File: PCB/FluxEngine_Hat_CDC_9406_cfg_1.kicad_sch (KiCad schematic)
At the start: 6 parts, among them J1 CY8CKIT-059, P1 FDD_IBMPC_host, P2 FDD_SA800_host

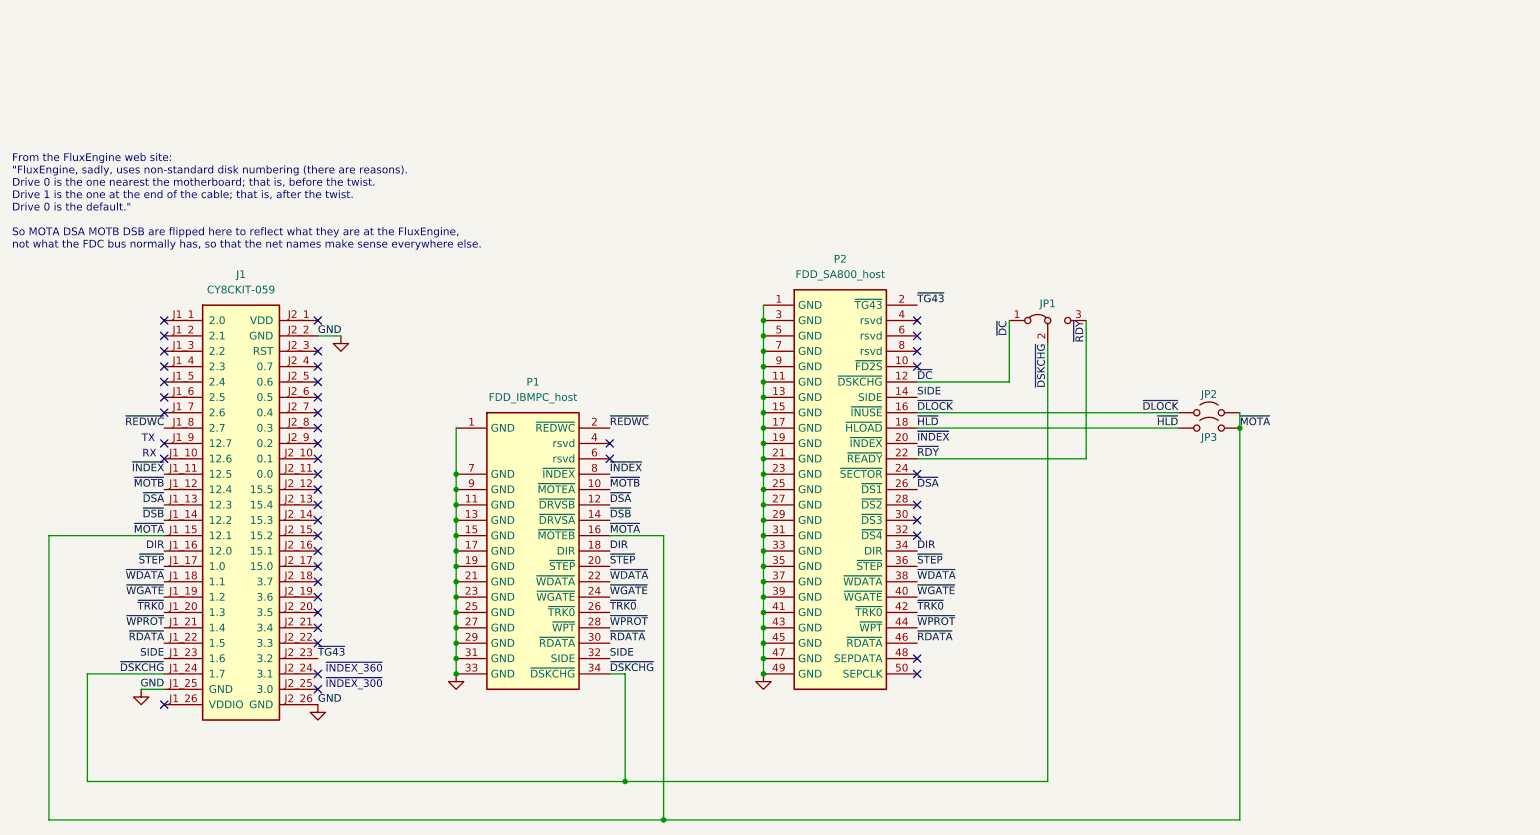
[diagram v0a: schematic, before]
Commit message: add CDC9406 type 1 & 2
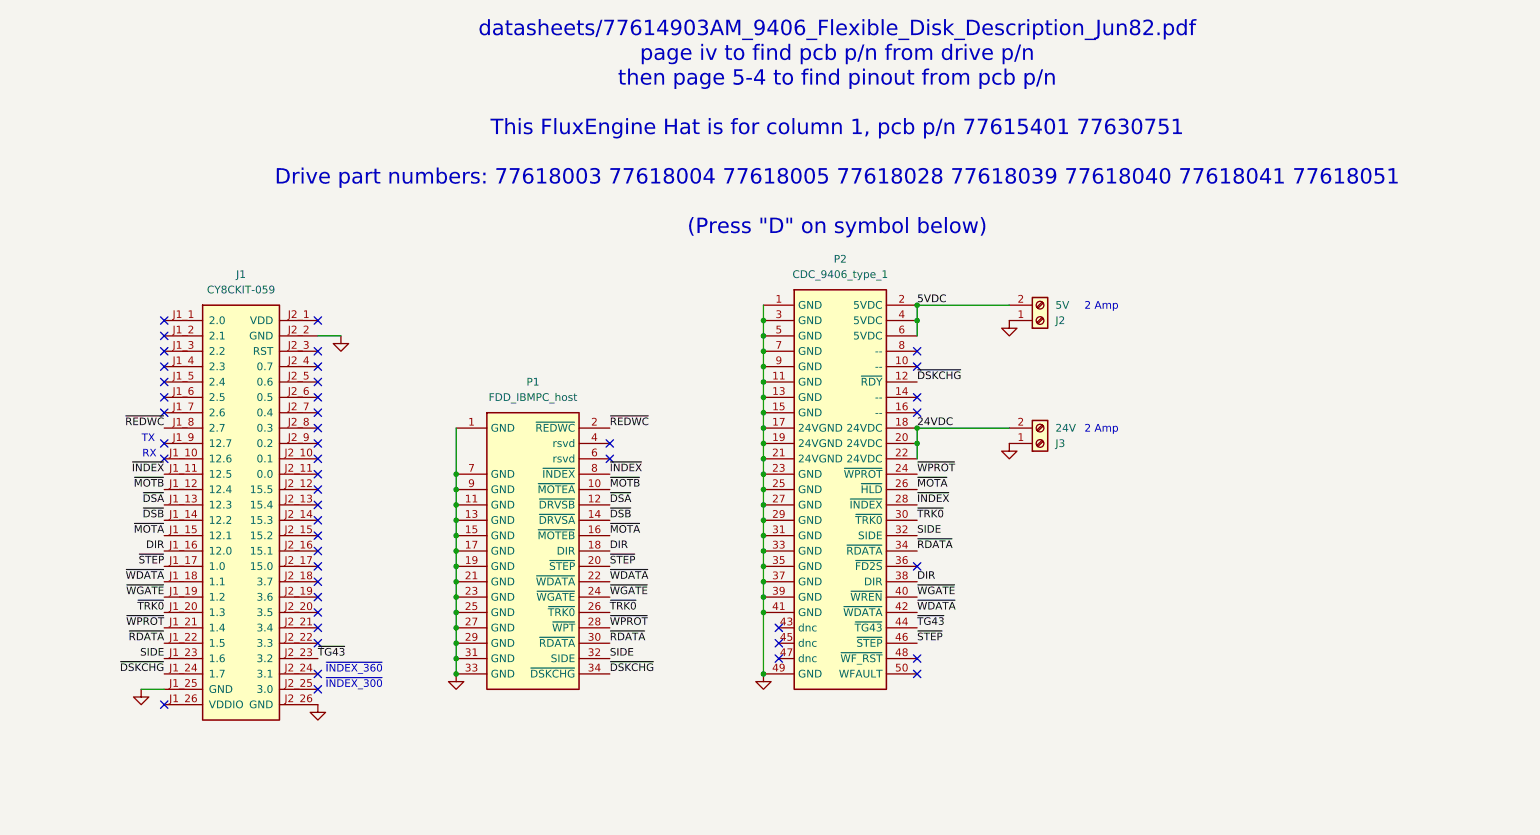
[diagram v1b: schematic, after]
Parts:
- removed JP1: Jumper_3_Bridged12, 000_LOCAL:PinHeader_1x03_P2.54mm_Vertical, symbol 000_LOCAL:Jumper_3_Bridged12
- removed JP2, JP3: Jumper_2_Open, 000_LOCAL:PinHeader_1x02_P2.54mm_Vertical, symbol 000_LOCAL:Jumper_2_Open
- added J2: 5V, 000_LOCAL:ScrewTerminal_1x02_P3.5mm_vertical, symbol 000_LOCAL:Screw_Terminal_01x02
- added J3: 24V, 000_LOCAL:ScrewTerminal_1x02_P3.5mm_vertical, symbol 000_LOCAL:Screw_Terminal_01x02
- P2: value FDD_SA800_host -> CDC_9406_type_1; symbol 000_LOCAL:FDD_SA800_host -> 000_LOCAL:FDD_CDC_9406_pinout_1
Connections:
- net ~{DC} is gone; now on net ~{DSKCHG}: P2.12 (~{RDY})
- net ~{RDY} is gone; now on net 24VDC: P2.22 (24VDC)
- net DIR: now also P2.38 (DIR); no longer P2.34 (DIR)
- net GND: now also J2.1 (Pin_1), J3.1 (Pin_1); no longer P2.43 (GND), P2.45 (GND), P2.47 (GND)
- net SIDE: now also P2.32 (SIDE); no longer P2.14 (SIDE)
- net ~{DSA}: no longer P2.26 (~{DS1})
- net ~{INDEX}: now also P2.28 (~{INDEX}); no longer P2.20 (~{INDEX})
- net ~{MOTA}: now also P2.26 (~{HLD})
- net ~{RDATA}: now also P2.34 (~{RDATA}); no longer P2.46 (~{RDATA})
- net ~{STEP}: now also P2.46 (~{STEP}); no longer P2.36 (~{STEP})
- net ~{TG43}: now also P2.44 (~{TG43}); no longer P2.2 (~{TG43})
- net ~{TRK0}: now also P2.30 (~{TRK0}); no longer P2.42 (~{TRK0})
- net ~{WDATA}: now also P2.42 (~{WDATA}); no longer P2.38 (~{WDATA})
- net ~{WPROT}: now also P2.24 (~{WPROT}); no longer P2.44 (~{WPT})
- net 5VDC: now reaches P2.4 (5VDC)
- net 5VDC: now also P2.2 (5VDC), P2.6 (5VDC), J2.2 (Pin_2)
- net ~{DLOCK}: no longer names the net of P2.16 (--)
- net ~{HLD} renamed 24VDC
- net 24VDC: now also P2.20 (24VDC), J3.2 (Pin_2)
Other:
- note added: "2 Amp"
- note added: "datasheets/77614903AM_9406_Flexible_Disk_Description_Jun82.pdf page iv to find pcb p/n from drive p/n then page 5-4 to find pinout from pcb p/n This FluxEngine Hat is for column 1, pcb p/n 77615401 77630751 Drive part numbers: 77618003 77618004 77618005 77618028 77618039 77618040 77618041 77618051 (Press "D" on symbol below)"
- note removed: "From the FluxEngine web site: "FluxEngine, sadly, uses non-standard disk numbering (there are reasons). Drive 0 is the one nearest the motherboard; that is, before the twist. Drive 1 is the one at the end of the cable; that is, after the twist. Drive 0 is the default." So MOTA DSA MOTB DSB are flipped here to reflect what they are at the FluxEngine, not what the FDC bus normally has, so that the 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"
- title: FluxEngine_Hat for PC and SA800 -> FluxEngine_Hat for PC and CDC-9406 cfg 1
